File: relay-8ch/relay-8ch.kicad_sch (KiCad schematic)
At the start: 31 parts, among them J101 Screw_Terminal_01x16, K101 FINDER-40.31, K102 FINDER-40.31, K103 FINDER-40.31, K104 FINDER-40.31, K105 FINDER-40.31, K106 FINDER-40.31, K107 FINDER-40.31, K108 FINDER-40.31, U101 74HC373

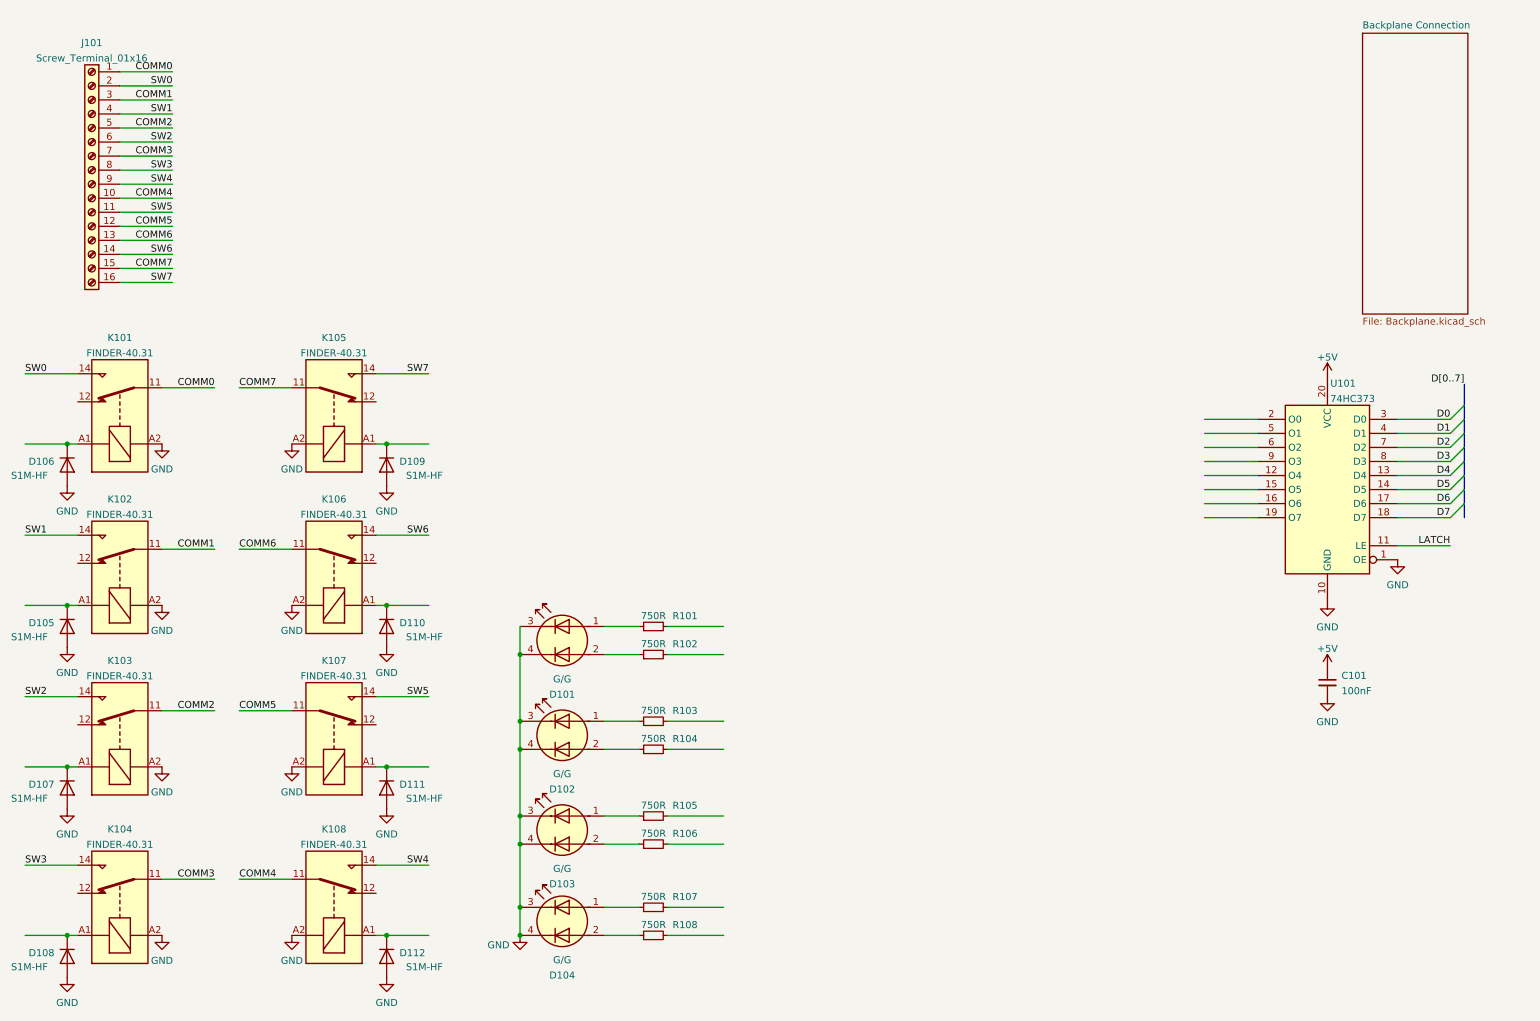
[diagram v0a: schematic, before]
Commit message: Finished routing relay board
- Completed routing of the relay board; it's got added an address
  selector switch and an I2C expander that can be used to set the
  address automatically.

- Minor tweaks to a few footprints, namely to make sure they're
  correctly tagged as through hole/SMD
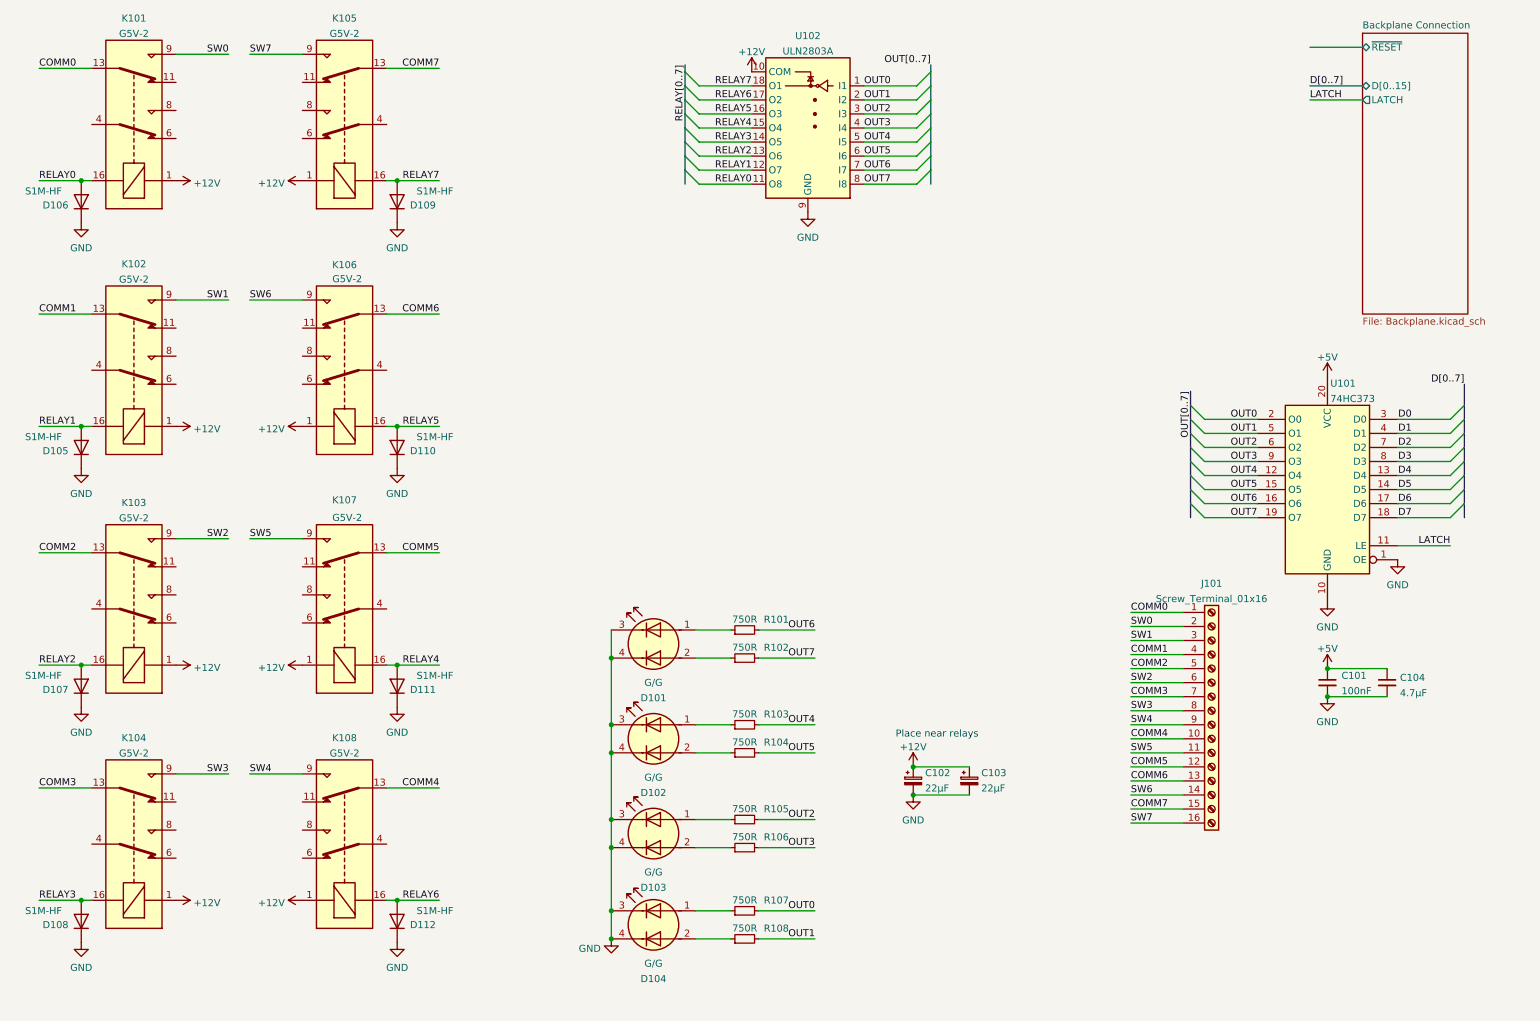
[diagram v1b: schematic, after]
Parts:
- added C102, C103: 22µF, Capacitor_THT:CP_Radial_D6.3mm_P2.50mm, symbol Device:C_Polarized_Small
- added C104: 4.7µF, Capacitor_SMD:C_0805_2012Metric, symbol Device:C_Small
- added U102: ULN2803A, Package_DIP:DIP-18_W7.62mm_Socket, symbol Transistor_Array:ULN2803A
- J101: MPN (none) -> 1843936
- K101, K102, K103, K104, K105, K106, K107, K108: value FINDER-40.31 -> G5V-2; footprint Relay_THT:Relay_SPDT_Finder_40.31 -> Relay_THT:Relay_DPDT_Omron_G5V-2; symbol Relay:FINDER-40.31 -> Relay:G5V-2
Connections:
- net +5V: now also C104.1
- net COMM0: now also K101.13; no longer K101.11
- net COMM1: now also J101.4 (Pin_4), K102.13; no longer J101.3 (Pin_3), K102.11
- net COMM2: now also K103.13; no longer K103.11
- net COMM3: now also K104.13; no longer K104.11
- net COMM4: now also K108.13; no longer K108.11
- net COMM5: now also K107.13; no longer K107.11
- net COMM6: now also K106.13; no longer K106.11
- net COMM7: now also K105.13; no longer K105.11
- net GND: now also D105.1 (K), D106.1 (K), D107.1 (K), D108.1 (K), D109.1 (K), D110.1 (K), D111.1 (K), D112.1 (K), C102.2, C103.2, C104.2, U102.9 (GND); no longer D105.2 (A), D106.2 (A), D107.2 (A), D108.2 (A), D109.2 (A), D110.2 (A), D111.2 (A), D112.2 (A), K101.A2, K102.A2, K103.A2, K104.A2, K105.A2, K106.A2, K107.A2, K108.A2
- net SW0: now also K101.9; no longer K101.14
- net SW1: now also J101.3 (Pin_3), K102.9; no longer J101.4 (Pin_4), K102.14
- net SW2: now also K103.9; no longer K103.14
- net SW3: now also K104.9; no longer K104.14
- net SW4: now also K108.9; no longer K108.14
- net SW5: now also K107.9; no longer K107.14
- net SW6: now also K106.9; no longer K106.14
- net SW7: now also K105.9; no longer K105.14
- net OUT4: now reaches R103.2
- net OUT4: now also U101.12 (O4), U102.5 (I5)
- net OUT3: now reaches R106.2
- net OUT3: now also U101.9 (O3), U102.4 (I4)
- net OUT0: now reaches R107.2
- net OUT0: now also U101.2 (O0), U102.1 (I1)
- net OUT5: now reaches U101.15 (O5)
- net OUT5: now also R104.2, U102.6 (I6)
- net OUT6: now reaches U101.16 (O6)
- net OUT6: now also R101.2, U102.7 (I7)
- net OUT7: now reaches U101.19 (O7)
- net OUT7: now also R102.2, U102.8 (I8)
- net OUT1: now reaches U101.5 (O1)
- net OUT1: now also R108.2, U102.2 (I2)
- net OUT2: now reaches U101.6 (O2)
- net OUT2: now also R105.2, U102.3 (I3)
- new net +12V: C102.1, C103.1, K101.1, K102.1, K103.1, K104.1, K105.1, K106.1, K107.1, K108.1, U102.10 (COM)
- new net RELAY0: D106.2 (A), K101.16, U102.11 (O8)
- new net RELAY1: D105.2 (A), K102.16, U102.12 (O7)
- new net RELAY2: D107.2 (A), K103.16, U102.13 (O6)
- new net RELAY3: D108.2 (A), K104.16, U102.14 (O5)
- new net RELAY4: D111.2 (A), K107.16, U102.15 (O4)
- new net RELAY5: D110.2 (A), K106.16, U102.16 (O3)
- new net RELAY6: D112.2 (A), K108.16, U102.17 (O2)
- new net RELAY7: D109.2 (A), K105.16, U102.18 (O1)
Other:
- sheet Backplane Connection ports: added D[0..15], LATCH, ~{RESET}; removed none
- note added: "Place near relays"
- moved on the sheet: D101, D102, D103, D104, D105, D106, D107, D108, D109, D110, D111, D112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

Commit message: Function codes, /DTACK for relay board
- Consider the state of the function code signals (so we don't decode
  CPU space cycles as accesses) and assert /DTACK when the latch signal
  is asserted. This should work for bus speeds of up to around 16MHz
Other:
- title: (none) -> 8 Channel Relay IO
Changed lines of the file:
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@@
 (kicad_sch (version 20211123) (generator eeschema)
   (paper "A4")
+  (title_block
+    (title "8 Channel Relay IO")
+    (date "2022-01-08")
+    (rev "1")
+    (comment 1 "NOTE: Not for switching mains!")
+  )
   (junction (at 124.46 182.88) (diameter 0) (color 0 0 0 0)
   )
@@
       (reference "#PWR0101") (unit 1) (value "GND") (footprint "")
     )
+    (path "/480e869c-5ccd-450b-826a-11fb4eb4f7b7/b692b8a2-428c-424f-b34e-d76890b7a7f8"
+      (reference "#PWR0102") (unit 1) (value "GND") (footprint "")
+    )
     (path "/480e869c-5ccd-450b-826a-11fb4eb4f7b7/752e8ff0-deb6-403f-a0be-46c7b2e2696e"
       (reference "#PWR0103") (unit 1) (value "+5V") (footprint "")
@@
       (reference "#PWR0135") (unit 1) (value "GND") (footprint "")
     )
+    (path "/480e869c-5ccd-450b-826a-11fb4eb4f7b7/b009b0eb-0f85-4729-91e1-917243f7809b"
+      (reference "#PWR0136") (unit 1) (value "GND") (footprint "")
+    )
     (path "/480e869c-5ccd-450b-826a-11fb4eb4f7b7/5feab5a5-9804-4bdb-b619-ab50ce0ad4ac"
       (reference "#PWR0201") (unit 1) (value "+5V") (footprint "")
@@
       (reference "#PWR0235") (unit 1) (value "GND") (footprint "")
     )
+    (path "/480e869c-5ccd-450b-826a-11fb4eb4f7b7/2380f0ea-c541-4606-be9d-2786c6ace66e"
+      (reference "#PWR0236") (unit 1) (value "+5V") (footprint "")
+    )
     (path "/480e869c-5ccd-450b-826a-11fb4eb4f7b7/088528ed-9597-4a2f-884e-b077d4d99f3c"
       (reference "#PWR0237") (unit 1) (value "+5V") (footprint "")
@@
       (reference "#PWR0241") (unit 1) (value "GND") (footprint "")
     )
+    (path "/480e869c-5ccd-450b-826a-11fb4eb4f7b7/204e4730-8a9c-4cdc-8fc7-1cf9cf4f7be0"
+      (reference "#PWR0242") (unit 1) (value "GND") (footprint "")
+    )
+    (path "/480e869c-5ccd-450b-826a-11fb4eb4f7b7/c55d54df-f0cb-49b0-a54e-4ba1e4d8c239"
+      (reference "#PWR0243") (unit 1) (value "+5V") (footprint "")
+    )
+    (path "/480e869c-5ccd-450b-826a-11fb4eb4f7b7/9243a53e-d8b5-4592-a915-9f51ee6e36a0"
+      (reference "#PWR0244") (unit 1) (value "GND") (footprint "")
+    )
     (path "/20540e7b-8f15-4bba-897f-079491897786"
       (reference "C101") (unit 1) (value "100nF") (footprint "Capacitor_SMD:C_0805_2012Metric")
@@
       (reference "U203") (unit 1) (value "MCP23008-xSO") (footprint "Package_SO:SOIC-18W_7.5x11.6mm_P1.27mm")
     )
-  )
+    (path "/480e869c-5ccd-450b-826a-11fb4eb4f7b7/ef8f89f8-ae63-4d88-a938-4c70414966d3"
+      (reference "U204") (unit 1) (value "74HC00") (footprint "Package_SO:SOIC-14_3.9x8.7mm_P1.27mm")
+    )
+    (path "/480e869c-5ccd-450b-826a-11fb4eb4f7b7/c1de4501-e1b6-4942-b001-88ab83f4db7c"
+      (reference "U204") (unit 2) (value "74HC00") (footprint "Package_SO:SOIC-14_3.9x8.7mm_P1.27mm")
+    )
+    (path "/480e869c-5ccd-450b-826a-11fb4eb4f7b7/c9352b75-69fa-4611-affb-e00a40f96633"
+      (reference "U204") (unit 3) (value "74HC00") (footprint "Package_SO:SOIC-14_3.9x8.7mm_P1.27mm")
+    )
+    (path "/480e869c-5ccd-450b-826a-11fb4eb4f7b7/a7236e94-0329-42b9-be93-82672d7507cb"
+      (reference "U204") (unit 4) (value "74HC00") (footprint "Package_SO:SOIC-14_3.9x8.7mm_P1.27mm")
+    )
+    (path "/480e869c-5ccd-450b-826a-11fb4eb4f7b7/4b34e7e6-48de-42b6-88c2-f39fe5a0e6a5"
+      (reference "U204") (unit 5) (value "74HC00") (footprint "Package_SO:SOIC-14_3.9x8.7mm_P1.27mm")
+    )
+    (path "/480e869c-5ccd-450b-826a-11fb4eb4f7b7/481a3c2b-bb6c-4af7-8ff1-3bad48f57666"
+      (reference "U205") (unit 1) (value "74LVC1G06") (footprint "68komputer-common:SC-74-5_1.5x2.9mm_P0.95mm")
+    )
+  )

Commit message: Minor tweaks to all boards
- Moved around some traces on the 68000 CPU card for prettiness

- Added a connector on the backplane to provide +5V/+12V without a
  management card installed (for testing)
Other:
- company: (none) -> Tristan Seifert
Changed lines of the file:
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@@
   (title_block
     (title "8 Channel Relay IO")
-    (date "2022-01-08")
+    (date "2022-01-09")
     (rev "1")
+    (company "Tristan Seifert")
     (comment 1 "NOTE: Not for switching mains!")
   )
@@
       (reference "U204") (unit 2) (value "74HC00") (footprint "Package_SO:SOIC-14_3.9x8.7mm_P1.27mm")
     )
-    (path "/480e869c-5ccd-450b-826a-11fb4eb4f7b7/c9352b75-69fa-4611-affb-e00a40f96633"
+    (path "/480e869c-5ccd-450b-826a-11fb4eb4f7b7/c9352b75-69fa-4611-affb-e00a40f96634"
       (reference "U204") (unit 3) (value "74HC00") (footprint "Package_SO:SOIC-14_3.9x8.7mm_P1.27mm")
     )

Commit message: Switched remaining pluggable screw terminals
- Replaced the pluggable/replaceable screw terminals with CUI devices
  parts on the backplane (+12V/GND/+5V) and relay board (switched
  contacts) since they're much cheaper and basically the same thing as
  the corresponding WE/Phoenix Contact parts
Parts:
- J101: footprint Connector_Phoenix_MC:PhoenixContact_MC_1,5_16-GF-3.5_1x16_P3.50mm_Horizontal_ThreadedFlange_MountHole -> 68komputer-common:CUI_TBP02R1W-381-16BE; MPN 1843936 -> TBP02R1W-381-16BE; MPN2 (none) -> TBP02P1W-381-16BE
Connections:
- net COMM0: now also J101.16 (Pin_16); no longer J101.1 (Pin_1)
- net COMM1: now also J101.13 (Pin_13); no longer J101.4 (Pin_4)
- net COMM2: now also J101.12 (Pin_12); no longer J101.5 (Pin_5)
- net COMM3: now also J101.10 (Pin_10); no longer J101.7 (Pin_7)
- net COMM4: now also J101.7 (Pin_7); no longer J101.10 (Pin_10)
- net COMM5: now also J101.5 (Pin_5); no longer J101.12 (Pin_12)
- net COMM6: now also J101.4 (Pin_4); no longer J101.13 (Pin_13)
- net COMM7: now also J101.2 (Pin_2); no longer J101.15 (Pin_15)
- net SW0: now also J101.15 (Pin_15); no longer J101.2 (Pin_2)
- net SW1: now also J101.14 (Pin_14); no longer J101.3 (Pin_3)
- net SW2: now also J101.11 (Pin_11); no longer J101.6 (Pin_6)
- net SW3: now also J101.9 (Pin_9); no longer J101.8 (Pin_8)
- net SW4: now also J101.8 (Pin_8); no longer J101.9 (Pin_9)
- net SW5: now also J101.6 (Pin_6); no longer J101.11 (Pin_11)
- net SW6: now also J101.3 (Pin_3); no longer J101.14 (Pin_14)
- net SW7: now also J101.1 (Pin_1); no longer J101.16 (Pin_16)
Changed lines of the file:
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@@
     (pin "1")
   )
-  (symbol (lib_id "Connector:Screw_Terminal_01x16") (at 233.045 141.605 0) (unit 1)
+  (symbol (lib_id "Connector:Screw_Terminal_01x16") (at 233.045 144.145 0) (mirror x) (unit 1)
     (in_bom yes) (on_board yes) (fields_autoplaced)
     (property "Reference" "J101" (id 0) (at 233.045 118.5885 0))
     (property "Value" "Screw_Terminal_01x16" (id 1) (at 233.045 121.3636 0))
-    (property "Footprint" "Connector_Phoenix_MC:PhoenixContact_MC_1,5_16-GF-3.5_1x16_P3.50mm_Horizontal_ThreadedFlange_MountHole" (id 2) (at 233.045 141.605 0)
-      (effects (font (size 1.27 1.27)) hide)
-    )
-    (property "Datasheet" "~" (id 3) (at 233.045 141.605 0)
-      (effects (font (size 1.27 1.27)) hide)
-    )
-    (property "MPN" "1843936" (id 4) (at 233.045 141.605 0)
+    (property "Footprint" "68komputer-common:CUI_TBP02R1W-381-16BE" (id 2) (at 233.045 144.145 0)
+      (effects (font (size 1.27 1.27)) hide)
+    )
+    (property "Datasheet" "~" (id 3) (at 233.045 144.145 0)
+      (effects (font (size 1.27 1.27)) hide)
+    )
+    (property "MPN" "TBP02R1W-381-16BE" (id 4) (at 233.045 144.145 0)
+      (effects (font (size 1.27 1.27)) hide)
+    )
+    (property "MPN2" "TBP02P1W-381-16BE" (id 5) (at 233.045 144.145 0)
       (effects (font (size 1.27 1.27)) hide)
     )
@@
     )
     (path "/cd5e5396-17e0-450e-8b9a-002266132cf2"
-      (reference "J101") (unit 1) (value "Screw_Terminal_01x16") (footprint "Connector_Phoenix_MC:PhoenixContact_MC_1,5_16-GF-3.5_1x16_P3.50mm_Horizontal_ThreadedFlange_MountHole")
+      (reference "J101") (unit 1) (value "Screw_Terminal_01x16") (footprint "68komputer-common:CUI_TBP02R1W-381-16BE")
     )
     (path "/480e869c-5ccd-450b-826a-11fb4eb4f7b7/bdd1c635-9dfb-4bc3-8ccf-d0f33d451f43"
